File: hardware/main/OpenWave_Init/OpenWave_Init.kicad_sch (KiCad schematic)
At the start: 12 parts, among them U1 AP7363-33D-13, U2 TPSM863257RDXR, U3 REF3333AIDBZR, U4 STM32H743VITx, U5 LMH6658MAX_NOPB, U6 LTC2642IMS-16#PBF

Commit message: Schematic, Design Changes
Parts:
- removed LDO1: TPS70933DBVR, easyeda2kicad:SOT-23-5_L3.0-W1.7-P0.95-LS2.8-BR, symbol easyeda2kicad:TPS70933DBVR
- added BT1: Battery_Cell, symbol Device:Battery_Cell
- added C1: 10uF, PCM_JLCPCB:C_CASE-A-3216-18(mm), symbol PCM_JLCPCB-Capacitors:CASE-A-3216-18(mm),10uF
- added C10, C9: 1pF, PCM_JLCPCB:C_0402, symbol PCM_JLCPCB-Capacitors:0402,1pF
- added C11, C16, C2, C21, C23, C3, C4, C5, C6: 100nF, PCM_JLCPCB:C_0402, symbol PCM_JLCPCB-Capacitors:0402,100nF,(2)
- added C12, C13, C15, C25: 10uF, PCM_JLCPCB:C_0603, symbol PCM_JLCPCB-Capacitors:0603,10uF,(2)
- added C14, C26: 22uF, PCM_JLCPCB:C_0805, symbol PCM_JLCPCB-Capacitors:0805,22uF
- added C17, C18, C22, C7: 1uF, PCM_JLCPCB:C_0402, symbol PCM_JLCPCB-Capacitors:0402,1uF
- added C19, C20: 4.7uF, PCM_JLCPCB:C_0603, symbol PCM_JLCPCB-Capacitors:0603,4.7uF
- added C24: 6.8pF, PCM_JLCPCB:C_0402, symbol PCM_JLCPCB-Capacitors:0402,6.8pF
- added C8: 2.2uF, PCM_JLCPCB:C_0603, symbol PCM_JLCPCB-Capacitors:0603,2.2uF
- added FB1, FB2, FB3, FB4: ~, PCM_JLCPCB:FB_0603, symbol PCM_JLCPCB-Inductors:Ferrite,0603
- added IC1: TPS7A2050PDBVR, SOT95P280X145-5N, symbol easyeda2kicad:TPS7A2050PDBVR
- added J2: SWD, symbol Connector_Generic:Conn_02x03_Odd_Even
- added JP1: SolderJumper, symbol Jumper:SolderJumper_2_Bridged
- added L1: 82uH,430mA, PCM_JLCPCB:L_SMD,4.5x4x3.2mm, symbol PCM_JLCPCB-Inductors:82uH,430mA
- added L3: 22uH,4.95A, PCM_JLCPCB:L_SMD,12.5x12.5mm, symbol PCM_JLCPCB-Inductors:22uH,4.95A
- added R1: 1.5kΩ, PCM_JLCPCB:R_0402, symbol PCM_JLCPCB-Resistors:0402,1.5kΩ
- added R2: 3.3kΩ, PCM_JLCPCB:R_0402, symbol PCM_JLCPCB-Resistors:0402,3.3kΩ
- added R3, R8: 10kΩ, PCM_JLCPCB:R_0402, symbol PCM_JLCPCB-Resistors:0402,10kΩ
- added R4: 220kΩ, PCM_JLCPCB:R_0402, symbol PCM_JLCPCB-Resistors:0402,220kΩ
- added R5: 150kΩ, PCM_JLCPCB:R_0402, symbol PCM_JLCPCB-Resistors:0402,150kΩ
- added R6: 100kΩ, PCM_JLCPCB:R_0402, symbol PCM_JLCPCB-Resistors:0402,100kΩ
- added R7: 30kΩ, PCM_JLCPCB:R_0603, symbol PCM_JLCPCB-Resistors:0603,30kΩ
- added R9: 4.7kΩ, PCM_JLCPCB:R_0402, symbol PCM_JLCPCB-Resistors:0402,4.7kΩ
- added SW1: Push_Button, Button_Switch_THT:SW_PUSH_6mm, symbol PCM_SL_Devices:Push_Button
- added X1: X322525MOB4SI, PCM_JLCPCB:OSC-SMD_4P-L3.2-W2.5-BL, symbol PCM_JLCPCB-Crystals:Crystal, 25MHz, 11pF
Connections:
- net +12V: now also U2.1 (VIN), C15.1, C16.1, R5.1
- net +3.3VA: now also R8.1; no longer U1.3 (OUT)
- net +3.3VDAC: now also U6.1 (REF), C19.1, C22.2, C23.2
- net +3V3: now also U1.3 (OUT), U4.100 (VDD), U4.11 (VDD), U4.27 (VDD), U4.50 (VDD), U4.75 (VDD), C1.1, C12.1, C2.1, C3.1, C4.1, C5.1, FB1.1, J2.1 (Pin_1), JP1.1 (A)
- net +5V: now also C13.1, C14.1, C17.1, C20.1, IC1.1 (IN), R4.1
- net GND: now also U4.10 (VSS), U4.19 (VSSA), U4.26 (VSS), U4.49 (VSS), U4.74 (VSS), U4.99 (VSS), U5.4 (V_-), BT1.2 (-), C1.2, C10.1, C11.1, C12.2, C13.2, C14.2, C15.2, C16.2, C17.2, C18.2, C19.2, C2.2, C20.2, C21.2, C22.1, C23.1, C25.2, C26.2, C3.2, C4.2, C5.2, C6.2, C7.2, C8.1, C9.1, IC1.2 (GND), J2.5 (Pin_5), R2.2, R6.2, R7.2, SW1.1, X1.2 (GND), X1.4 (GND)
- net at U2.6 (EN): now also R5.2, R6.1
- net at U2.7 (FB): now also R4.2, R7.1
- net at U5.1 (OUT_A): now also U5.2 (-IN_A)
- net at U5.6 (-IN_B): now also U5.7 (OUT_B)
- net at U5.8 (V_+): now also FB4.2
- net at U4.12 (PH0): now also C10.2, X1.3 (OSC)
- net at U4.13 (PH1): now also C9.2, X1.1 (OSC)
- net uC_SW_NRST: now reaches U4.14 (NRST)
- net uC_SW_NRST: now also C11.2, J2.3 (Pin_3), SW1.2
- net +3.3VA_uC: now reaches U4.20 (VREF+)
- net +3.3VA_uC: now also U4.21 (VDDA), C6.1, C7.1, FB1.2
- net at U4.48 (VCAP): now also U4.73 (VCAP), C8.2
- net at U4.6 (VBAT): now also BT1.1 (+), JP1.2 (B)
- net uC_USB_VBUS: now reaches U4.68 (PA9)
- net uC_USB_VBUS: now also R1.1, R2.1
- net uC_USB_D-: now reaches U4.70 (PA11)
- net uC_USB_D+: now reaches U4.71 (PA12)
- net uC_SW_DIO: now reaches U4.72 (PA13)
- net uC_SW_DIO: now also J2.2 (Pin_2)
- net uC_SW_CLK: now reaches U4.76 (PA14)
- net uC_SW_CLK: now also J2.4 (Pin_4)
- net uC_SW_O: now reaches U4.89 (PB3)
- net uC_SW_O: now also J2.6 (Pin_6)
- net at U4.94 (BOOT0): now also R3.2
- net uC_SPI_CS: now reaches U6.2 (~{CS})
- net uC_SPI_CLK: now reaches U6.3 (SCLK)
- net uC_SPI_MOSI: now reaches U6.4 (DIN)
- net at U6.5 (~{CLR}): now also R8.2
- net at U6.7 (INV): now also C24.1
- net at U6.8 (RFB): now also C24.2
- net at U6.9 (VDD): now also C21.1, FB2.2
- new net: C25.1, FB3.2, L3.1
- new net: C18.1, FB3.1, IC1.5 (OUT)
- new net: IC1.3 (EN), R9.1
- new net +5VA: C26.1, FB2.1, FB4.1, L3.2
- new net LDO_5VA_EN: R9.2
- new net USB_VBUS: R1.2
- new net uC_SW_BOOT0: R3.1
- no-connect marks 1 -> 0
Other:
- note added: "10kHz Cut-Off"
- note added: "Analog Voltage"
- note added: "Digital Voltage"
- note added: "General Voltage"
- note added: "Reference Voltage"
- note added: "System VIN"
- moved on the sheet: U1, U2, U3, U4, U5

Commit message: V0.2
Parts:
- removed C10, C9: 1pF, PCM_JLCPCB:C_0402, symbol PCM_JLCPCB-Capacitors:0402,1pF
- removed C22: 1uF, PCM_JLCPCB:C_0402, symbol PCM_JLCPCB-Capacitors:0402,1uF
- removed C24: 6.8pF, PCM_JLCPCB:C_0402, symbol PCM_JLCPCB-Capacitors:0402,6.8pF
- removed L1: 82uH,430mA, PCM_JLCPCB:L_SMD,4.5x4x3.2mm, symbol PCM_JLCPCB-Inductors:82uH,430mA
- removed R4: 220kΩ, PCM_JLCPCB:R_0402, symbol PCM_JLCPCB-Resistors:0402,220kΩ
- removed SW1: Push_Button, Button_Switch_THT:SW_PUSH_6mm, symbol PCM_SL_Devices:Push_Button
- added C18: 22uF, PCM_JLCPCB:C_0805, symbol PCM_JLCPCB-Capacitors:0805,22uF
- added C24, C25, C26, C42, C46: 100pF, PCM_JLCPCB:C_0402, symbol PCM_JLCPCB-Capacitors:0402,100pF
- added C28: 1uF, PCM_JLCPCB:C_0402, symbol PCM_JLCPCB-Capacitors:0402,1uF
- added C29, C30, C37, C38, C48, C55, C56, C57, C58, C59, C60, C61: 100nF, PCM_JLCPCB:C_0402, symbol PCM_JLCPCB-Capacitors:0402,100nF,(2)
- added C32, C33, C51, C63: 10nF, PCM_JLCPCB:C_0402, symbol PCM_JLCPCB-Capacitors:0402,10nF
- added C34: 10uF, PCM_JLCPCB:C_CASE-A-3216-18(mm), symbol PCM_JLCPCB-Capacitors:CASE-A-3216-18(mm),10uF
- added C35, C39, C54, C62: 10uF, PCM_JLCPCB:C_0603, symbol PCM_JLCPCB-Capacitors:0603,10uF,(2)
- added C36: 2.2uF, PCM_JLCPCB:C_0603, symbol PCM_JLCPCB-Capacitors:0603,2.2uF
- added C40, C47: 220nF, PCM_JLCPCB:C_0402, symbol PCM_JLCPCB-Capacitors:0402,220nF
- added C41, C45: 1.5nF, PCM_JLCPCB:C_0603, symbol PCM_JLCPCB-Capacitors:0603,1.5nF
- added C43, C44: 680pF, PCM_JLCPCB:C_0402, symbol PCM_JLCPCB-Capacitors:0402,100pF
- added C49, C50: 6.8pF, PCM_JLCPCB:C_0402, symbol PCM_JLCPCB-Capacitors:0402,6.8pF
- added C52, C53: 15pF, PCM_JLCPCB:C_0402, symbol PCM_JLCPCB-Capacitors:0402,15pF
- added C64: 4.7uF, PCM_JLCPCB:C_0603, symbol PCM_JLCPCB-Capacitors:0603,4.7uF
- added C8, C9: 10pF, PCM_JLCPCB:C_0402, symbol PCM_JLCPCB-Capacitors:0402,10pF
- added D1: LED, LED_SMD:LED_0603_1608Metric, symbol PCM_SL_Devices:LED
- added D2: SMAJ10CA, PCM_JLCPCB:D_SMA, symbol PCM_JLCPCB-Diodes:TVS-Bi,SMAJ10CA
- added D3, D4, D5, D6, D7: TPRCLAMP2451ZA, PCM_JLCPCB:D_DFN0603-2, symbol PCM_JLCPCB-Diodes:TVS-Bi,TPRCLAMP2451ZA
- added FB4, FB7: ~, PCM_JLCPCB:FB_0603, symbol PCM_JLCPCB-Inductors:Ferrite,0603
- added FB6: ~, PCM_JLCPCB:FB_0805, symbol PCM_JLCPCB-Inductors:Ferrite,0805
- added FL1: ACT1210D-101-2P-TL00, A Lot of Stuff:ACT1210D1012PTL00, symbol Device:Filter_EMI_LL_1423
- added FL2: Choke_Coilcraft_0603USB-222, Inductor_SMD:L_CommonModeChoke_Coilcraft_0603USB, symbol Filter:Choke_Coilcraft_0603USB-222
- added J1: UART, Connector_PinHeader_2.54mm:PinHeader_1x02_P2.54mm_Vertical, symbol Connector_Generic:Conn_01x02
- added J3: FPC 6S, Connector_FFC-FPC:Hirose_FH12-6S-0.5SH_1x06-1MP_P0.50mm_Horizontal, symbol Connector_Generic_MountingPin:Conn_01x06_MountingPin
- added J4: Barrel_Jack_Switch_MountingPin, A Lot of Stuff:PRT10811, symbol Connector:Barrel_Jack_Switch_MountingPin
- added J5: Control_In, Connector_JST:JST_XH_S2B-XH-A-1_1x02_P2.50mm_Horizontal, symbol Connector_Generic:Conn_01x02
- added J6, J7: BNC, A Lot of Stuff:5415025-2, symbol Connector:Conn_Coaxial
- added J8: USB_C_Receptacle_USB2.0_16P, Connector_USB:USB_C_Receptacle_GCT_USB4105-xx-A_16P_TopMnt_Horizontal, symbol Connector:USB_C_Receptacle_USB2.0_16P
- added J9: RB1-125BAG1A, RB1125BAG1A, symbol _custom:RB1-125BAG1A
- added JP2: Termination Jumper, Jumper:SolderJumper-2_P1.3mm_Open_Pad1.0x1.5mm, symbol Jumper:Jumper_2_Open
- added R12, R26, R29: 120Ω, PCM_JLCPCB:R_0402, symbol PCM_JLCPCB-Resistors:0402,120Ω
- added R13, R17: 10kΩ, PCM_JLCPCB:R_0402, symbol PCM_JLCPCB-Resistors:0402,10kΩ
- added R15, R16: 5.1kΩ, PCM_JLCPCB:R_0402, symbol PCM_JLCPCB-Resistors:0402,5.1kΩ
- added R18: 100Ω, PCM_JLCPCB:R_0603, symbol PCM_JLCPCB-Resistors:0603,100Ω
- added R19, R20: 33Ω, PCM_JLCPCB:R_0402, symbol PCM_JLCPCB-Resistors:0402,33Ω
- added R21, R22, R23, R24, R33, R34, R38, R39: 49.9Ω, PCM_JLCPCB:R_0402, symbol PCM_JLCPCB-Resistors:0402,49.9Ω
- added R25, R32: 1Ω, PCM_JLCPCB:R_0402, symbol PCM_JLCPCB-Resistors:0402,1Ω
- added R27, R30: 1.2kΩ, PCM_JLCPCB:R_0402, symbol PCM_JLCPCB-Resistors:0402,1.2kΩ
- added R28, R31: 360Ω, PCM_JLCPCB:R_0603, symbol PCM_JLCPCB-Resistors:0603,360Ω
- added R35: 10Ω, PCM_JLCPCB:R_0402, symbol PCM_JLCPCB-Resistors:0402,10Ω
- added R36, R37: 220Ω, PCM_JLCPCB:R_0402, symbol PCM_JLCPCB-Resistors:0402,220Ω
- added R4, R42: 330Ω, PCM_JLCPCB:R_0402, symbol PCM_JLCPCB-Resistors:0402,330Ω
- added R40: 1MΩ, PCM_JLCPCB:R_0402, symbol PCM_JLCPCB-Resistors:0402,1MΩ
- added R41: 12kΩ, PCM_JLCPCB:R_0402, symbol PCM_JLCPCB-Resistors:0402,12kΩ
- added R43: 75Ω, PCM_JLCPCB:R_0402, symbol PCM_JLCPCB-Resistors:0402,75Ω
- added R5, R6: 4.7kΩ, PCM_JLCPCB:R_0402, symbol PCM_JLCPCB-Resistors:0402,4.7kΩ
- added R7: 240kΩ, PCM_JLCPCB:R_0603, symbol PCM_JLCPCB-Resistors:0603,240kΩ
- added U10, U9: TMP100, Package_TO_SOT_SMD:SOT-23-6, symbol Sensor_Temperature:TMP100
- added U11: USBLC6-2P6, Package_TO_SOT_SMD:SOT-666, symbol Power_Protection:USBLC6-2P6
- added U12: W25Q128, PCM_JLCPCB:SOIC-8_L5.3-W5.3-P1.27-LS8.0-BL, symbol PCM_JLCPCB-Memory:16MByte, SPI
- added U13: SN74LVC8T245, easyeda2kicad:VQFN-24_L5.6-W3.6-P0.50-BL-EP, symbol Logic_LevelTranslator:SN74LVC8T245
- added U14: W5500, Package_QFP:LQFP-48_7x7mm_P0.5mm, symbol Interface_Ethernet:W5500
- added U5: TJA1051T-3, Package_SO:SOIC-8_3.9x4.9mm_P1.27mm, symbol Interface_CAN_LIN:TJA1051T-3
- added U6: LTC2642IMS-16#PBF, easyeda2kicad:MSOP-10_L3.0-W3.0-P0.50-LS4.9-BL, symbol easyeda2kicad:LTC2642IMS-16#PBF
- added X2: X322525MOB4SI, PCM_JLCPCB:OSC-SMD_4P-L3.2-W2.5-BL, symbol PCM_JLCPCB-Crystals:Crystal, 25MHz, 11pF
- BT1: footprint (none) -> Battery:Battery_Panasonic_CR1220-VCN_Vertical_CircularHoles
- IC1: footprint SOT95P280X145-5N -> easyeda2kicad:SOT95P280X145-5N
- J2: footprint (none) -> Connector_PinHeader_1.00mm:PinHeader_2x03_P1.00mm_Vertical
- JP1: footprint (none) -> Jumper:SolderJumper-2_P1.3mm_Bridged2Bar_Pad1.0x1.5mm
- L1: renamed from L3; value 22uH,4.95A -> 22uH, 340mA; footprint PCM_JLCPCB:L_SMD,12.5x12.5mm -> Inductor_SMD:L_1210_3225Metric; LCSC C2924827 -> DNP; Manufacturer SXN(Shun Xiang Nuo Elec) -> Bourns; Part SMDRI129-220MT -> SRN2012T-220K
- U7: renamed from U5; footprint SOIC127P600X175-8N -> A Lot of Stuff:SOIC127P600X175-8N
- renumbered C7 to C1, C8 to C10, C13 to C12, C12 to C13, C15 to C14, C16 to C15, C17 to C16, C14 to C17, C18 to C19, C6 to C2, C25 to C20, C26 to C21, C19 to C22, C20 to C23, C23 to C27, C5 to C3, C21 to C31, C3 to C5, C2 to C6, C1 to C7, FB3 to FB2, FB4 to FB3, FB2 to FB5, R3 to R1, R9 to R10, R6 to R11, R8 to R14, R1 to R2, R2 to R3, R5 to R8, R7 to R9, U4 to U1, U1 to U2, U2 to U3, U3 to U4, U6 to U8
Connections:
- net +12V: now also C35.1, FB6.2
- net +3.3VA: no longer R14.1
- net +3.3VDAC: now also R14.1, U8.7 (INV), U8.8 (RFB), C28.2, C29.2, R13.1, U6.1 (REF), U6.7 (INV), U6.8 (RFB)
- net +3V3: now also C26.1, C32.1, C33.1, C37.1, C39.1, C54.1, C55.1, D7.2, FB7.1, J3.1 (Pin_1), J9.L1 (A_YELLOW), J9.L3 (A_GREEN), R33.1, R34.1, R35.1, U10.4 (V+), U10.5 (ADD0), U12.8 (VCC), U13.1 (V_{CCA}), U14.28 (VDD), U5.5 (VIO), U9.4 (V+)
- net +5V: no longer C12.1, C16.1, C17.1, C23.1, IC1.1 (IN), U2.1 (IN), U3.3 (VOUT), U4.1 (IN)
- net +5VA: now also FB4.1, U13.23 (V_{CCB}), U13.24 (V_{CCB})
- net GND: now also C18.2, C24.2, C25.1, C26.2, C28.1, C29.1, C30.2, C32.2, C33.2, C34.2, C35.2, C36.1, C37.2, C38.2, C39.2, C40.2, C41.2, C42.2, C45.2, C46.2, C47.2, C48.2, C51.2, C52.1, C53.2, C54.2, C55.2, C56.2, C57.2, C58.2, C59.2, C60.2, C61.2, C62.2, C63.2, C64.2, C8.1, C9.2, D1.1, D2.2, D3.1, D4.1, D5.1, D6.1, D7.1, J3.6 (Pin_6), J3.MP (MountPin), J4.2, J4.MP (MountPin), J6.2 (Ext), J7.2 (Ext), J8.A1 (GND), J8.A12 (GND), J8.B1 (GND), J8.B12 (GND), J8.S1 (SHIELD), J9.1 (SHIELD_1), J9.2 (SHIELD_2), R15.1, R16.1, R17.2, R43.2, U10.2 (GND), U10.3 (ADD1), U11.2 (GND), U12.4 (GND), U13.11 (GND), U13.12 (GND), U13.13 (GND), U14.14 (AGND), U14.16 (AGND), U14.19 (AGND), U14.29 (GND), U14.3 (AGND), U14.48 (AGND), U14.9 (AGND), U5.2 (GND), U6.10 (GND), U9.2 (GND), U9.3 (ADD1), U9.5 (ADD0), X2.2 (GND), X2.4 (GND)
- net uC_SPI_CLK: now also R19.1, U13.4 (A2); no longer U8.3 (SCLK)
- net uC_SPI_CS: now also U1.41 (PE11), U13.3 (A1); no longer U8.2 (~{CS})
- net uC_SPI_MOSI: now also U1.44 (PE14), U13.5 (A3); no longer U8.4 (DIN)
- net uC_SW_CLK: now also R22.2; no longer J2.4 (Pin_4)
- net uC_SW_DIO: now also R23.2; no longer J2.2 (Pin_2)
- net uC_SW_NRST: now also R24.2; no longer C11.2, J2.3 (Pin_3)
- net uC_SW_O: now also R21.2; no longer J2.6 (Pin_6)
- net uC_USB_D+: now also FL2.2
- net uC_USB_D-: now also FL2.3
- net at BT1.1 (+), JP1.2 (B), U1.6 (VBAT): now also C38.1
- net at R9.1, U3.7 (FB): now also R7.1
- net at U1.13 (PH1), X1.1 (OSC): now also C9.1
- net at U1.12 (PH0), X1.3 (OSC): now also C8.2
- net Wave_OUTA: now reaches U7.1 (OUT_A), U7.2 (-IN_A)
- net Wave_OUTA: now also C43.2, R25.1
- net at U7.3 (+IN_A): now also C42.1, R28.2
- net at U7.5 (+IN_B): now also C46.1, R31.2
- net Wave_OUTB: now reaches U7.6 (-IN_B), U7.7 (OUT_B)
- net Wave_OUTB: now also C44.2, R32.1
- net uc_QSPI_IO2: now reaches U1.1 (PE2)
- net uc_QSPI_IO2: now also U12.3 (IO2)
- net W55_SPI2_MISO: now reaches U1.16 (PC1)
- net W55_SPI2_MISO: now also U14.34 (MISO)
- net W55_SPI2_MOSI: now reaches U1.17 (PC2_C)
- net W55_SPI2_MOSI: now also U14.35 (MOSI)
- net uC_SPI2_CS: now reaches U1.28 (PA4)
- net uC_SPI2_CS: now also U13.8 (A6)
- net at U1.29 (PA5): now also R20.2
- net uC_SPI2_MOSI: now reaches U1.31 (PA7)
- net uC_SPI2_MOSI: now also U13.10 (A8)
- net uc_QSPI_CLK: now reaches U1.36 (PB2)
- net uc_QSPI_CLK: now also U12.6 (CLK)
- net at U1.42 (PE12): now also R19.2
- net uc_QSPI_CS: now reaches U1.46 (PB10)
- net uc_QSPI_CS: now also U12.1 (CS#)
- net at C10.2, U1.73 (VCAP): no longer U1.48 (VCAP)
- net uc_QSPI_IO0: now reaches U1.58 (PD11)
- net uc_QSPI_IO0: now also U12.5 (DI)
- net uc_QSPI_IO1: now reaches U1.59 (PD12)
- net uc_QSPI_IO1: now also U12.2 (DO)
- net uc_QSPI_IO3: now reaches U1.60 (PD13)
- net uc_QSPI_IO3: now also U12.7 (IO3)
- net uC_SPI3_CS: now reaches U1.77 (PA15)
- net uC_SPI3_CS: now also J3.2 (Pin_2)
- net uC_SPI3_CLK: now reaches U1.78 (PC10)
- net uC_SPI3_CLK: now also J3.3 (Pin_3)
- net uC_SPI3_MISO: now reaches U1.79 (PC11)
- net uC_SPI3_MISO: now also J3.4 (Pin_4)
- net uC_SPI3_MOSI: now reaches U1.80 (PC12)
- net uC_SPI3_MOSI: now also J3.5 (Pin_5)
- net uC_CAN_RX: now reaches U1.81 (PD0)
- net uC_CAN_RX: now also U5.4 (RXD)
- net uC_CAN_TX: now reaches U1.82 (PD1)
- net uC_CAN_TX: now also U5.1 (TXD)
- net W55_SPI2_SCK: now reaches U1.84 (PD3)
- net W55_SPI2_SCK: now also U14.33 (SCLK)
- net W55_SPI2_CS: now reaches U1.96 (PB9)
- net W55_SPI2_CS: now also U14.32 (~{SCS})
- net at U8.6 (VOUT): now also R29.1
- net LDO_5VA_EN: no longer names the net of R10.2
- net LDO_5VA_EN: now also C16.1, IC1.1 (IN), C34.1, R18.2
- net USB_VBUS renamed +5V_USB
- net +5V_USB: now also J8.A4 (VBUS), J8.A9 (VBUS), J8.B4 (VBUS), J8.B9 (VBUS), U11.5 (VBUS)
- net uC_SW_BOOT0 renamed uC_BOOT0
- new net: C11.2, D6.2, J2.3 (Pin_3), R24.1
- new net: D4.2, J2.4 (Pin_4), R22.1
- new net: C43.1, R27.2, R28.1
- new net: C40.1, J6.1 (In), R25.2
- new net: C56.1, C57.1, C58.1, C59.1, C60.1, C61.1, C62.1, FB7.2, U14.11 (AVDD), U14.15 (AVDD), U14.17 (AVDD), U14.21 (AVDD), U14.4 (AVDD), U14.8 (AVDD)
- new net: C53.1, R40.2, U14.31 (XO), X2.1 (OSC)
- new net: J8.A7 (D-), J8.B7 (D-), U11.1 (I/O1)
- new net: J8.A6 (D+), J8.B6 (D+), U11.3 (I/O2)
- new net: FL2.1, U11.4 (I/O2)
- new net: FL2.4, U11.6 (I/O1)
- new net: C44.1, R30.2, R31.1
- new net: C30.1, FB4.2, U6.9 (VDD)
- new net: C41.1, R26.2, R27.1
- new net: C51.1, R38.2, R39.2
- new net: C45.1, R29.2, R30.1
- new net: C50.1, R39.1, U14.5 (RXN)
- new net: C50.2, J9.R8 (RD-)
- new net: C63.1, U14.22 (1V2O)
- new net: C49.1, R38.1, U14.6 (RXP)
- new net: D5.2, J2.2 (Pin_2), R23.1
- new net: C52.2, R40.1, U14.30 (XI/CLKIN), X2.3 (OSC)
- new net: D2.1, FB6.1, J4.1
- new net: J9.R1 (TD+), R33.2, U14.2 (TXP)
- new net: C36.2, U1.48 (VCAP)
- new net: J9.L2 (K_YELLOW), R36.2
- new net: JP2.1 (A), R12.1
- new net: R13.2, U6.5 (~{CLR})
- new net: R26.1, U6.6 (VOUT)
- new net: FL1.3, J5.1 (Pin_1)
- new net: FL1.4, J5.2 (Pin_2)
- new net: J8.A5 (CC1), R15.2
- new net: J9.R2 (TD-), R34.2, U14.1 (TXN)
- new net: R41.1, U14.10 (EXRES1)
- new net: C64.1, U14.20 (TOCAP)
- new net: D3.2, J2.6 (Pin_6), R21.1
- new net: C47.1, J7.1 (In), R32.2
- new net: R41.2, R42.1
- new net: R42.2, R43.1
- new net: D1.2, R4.2
- new net: J8.A8 (SBU1), J8.B8 (SBU2), R17.1
- new net: C48.1, J9.R3 (CT), R35.2
- new net: J9.L4 (K_GREEN), R37.2
- new net: C49.2, J9.R7 (RD+)
- new net: J8.B5 (CC2), R16.2
- new net +5.5V: C12.1, C17.1, C18.1, C23.1, R18.1, R7.2, U2.1 (IN), U3.3 (VOUT), U4.1 (IN), U5.3 (VCC)
- new net ACT_LED: R37.1, U14.27 (ACTLED)
- new net CAN_H: C24.1, FL1.1, JP2.2 (B), U5.7 (CANH)
- new net CAN_L: C25.2, FL1.2, R12.2, U5.6 (CANL)
- new net DAC_SPI2_CLK: U13.15 (B7), U6.3 (SCLK)
- new net DAC_SPI2_CS: U13.16 (B6), U6.2 (~{CS})
- new net DAC_SPI2_MOSI: U13.14 (B8), U6.4 (DIN)
- new net DAC_SPI_CLK: U13.20 (B2), U8.3 (SCLK)
- new net DAC_SPI_CS: U13.21 (B1), U8.2 (~{CS})
- new net DAC_SPI_MOSI: U13.19 (B3), U8.4 (DIN)
- new net LINK_LED: R36.1, U14.25 (LINKLED)
- new net LLT_DIR: U13.2 (DIR)
- new net LLT_OE: U13.22 (~{OE})
- new net W55_INT: U14.36 (~{INT})
- new net W55_RST: U14.37 (~{RST})
- new net uC_CAN_SILENT: U5.8 (S)
- new net uC_I2C_SCL: R6.2, U10.1 (SCL), U9.1 (SCL)
- new net uC_I2C_SDA: R5.2, U10.6 (SDA), U9.6 (SDA)
- new net uC_SPI2_CLK: R20.1, U13.9 (A7)
- new net uC_UART_RX: J1.1 (Pin_1)
- new net uC_UART_TX: J1.2 (Pin_2)
- no-connect marks 0 -> 15
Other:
- note added: "1001000"
- note added: "1001010"
- note added: "11 pF Crystal 5-7 pF stray from STM"
- note added: "11 pf Crystal 7.5 pf caps 3-4 pf stray"
- note added: "15W"
- note added: "CAN-BUS"
- note added: "Close to Connector"
- note added: "DAC, OPAMP"
- note added: "Do not ask. =12.4k"
- note added: "Logic Level 5-3.3"
- note added: "Memory"
- note added: "POWER"
- note added: "Temp."
- note added: "UI Board Conn"
- note added: "USB"
- note added: "fc = 725-800kHz"
- note added: "fc = 906 , 916 kHz ζ = 0.49 f = 795 kHz"
- note added: "uC"
- moved on the sheet: BT1, C1, C10, C11, C12, C13, C14, C15, C16, C17, C19, C2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

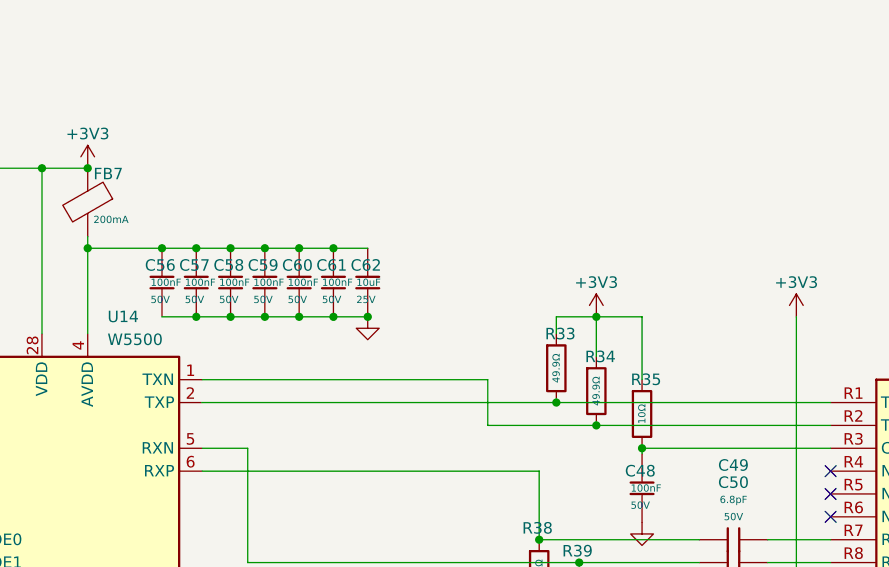
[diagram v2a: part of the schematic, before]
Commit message: WA5500 implementation
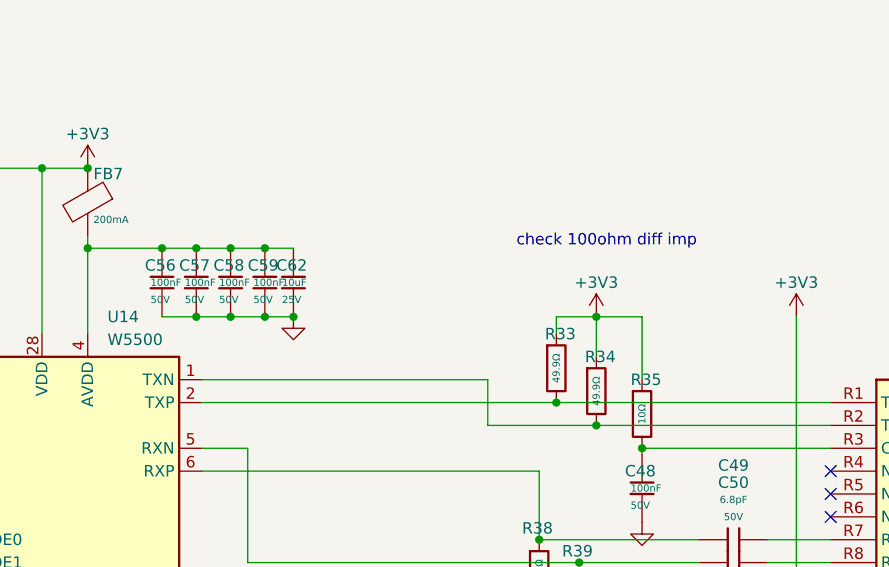
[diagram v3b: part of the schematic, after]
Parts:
- removed C60, C61: 100nF, PCM_JLCPCB:C_0402, symbol PCM_JLCPCB-Capacitors:0402,100nF,(2)
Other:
- note added: "check 100ohm diff imp"
- moved on the sheet: C62

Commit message: fixed ethernet, impedance, new swiftcircuit logo, arranged schematic
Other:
- moved on the sheet: C27, C28, C29, C30, C31, C40, C41, C42, C43, C44, C45, C46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
